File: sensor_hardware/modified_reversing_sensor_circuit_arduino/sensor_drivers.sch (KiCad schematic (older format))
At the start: 26 parts, among them Q1 S8050-J3Y, Q2 S8050-J3Y, Q3 S8050-J3Y, Q4 S8050-J3Y, U3 4052

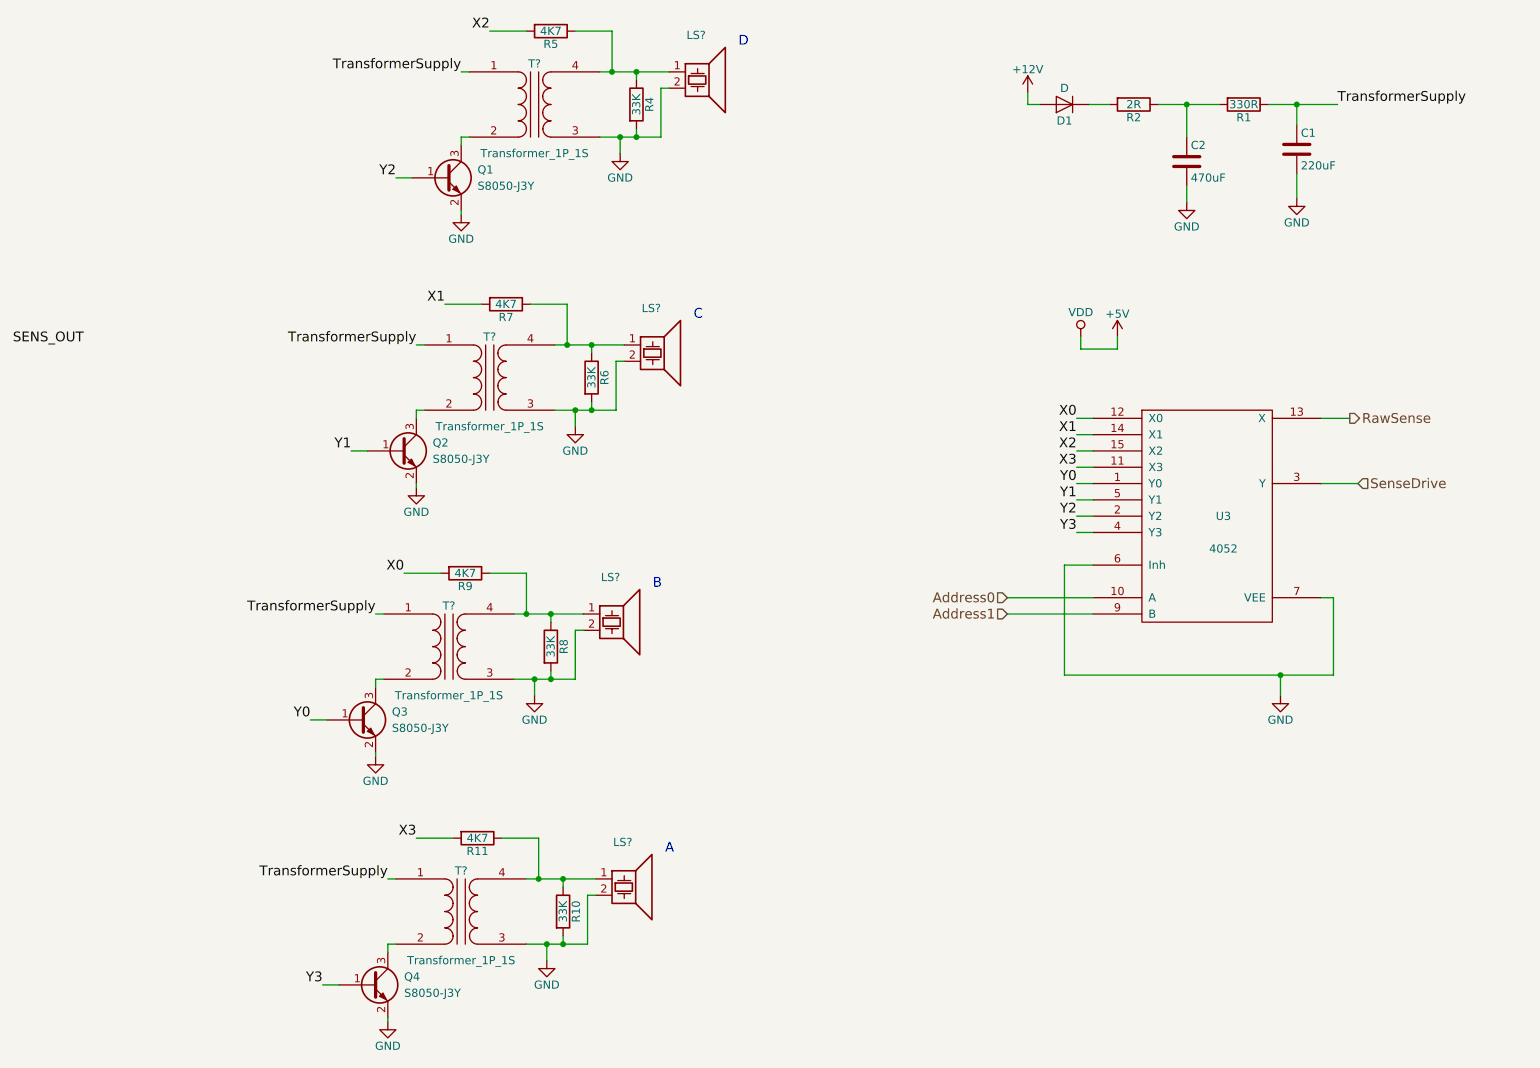
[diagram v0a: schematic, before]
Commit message: make specific atmega328 version
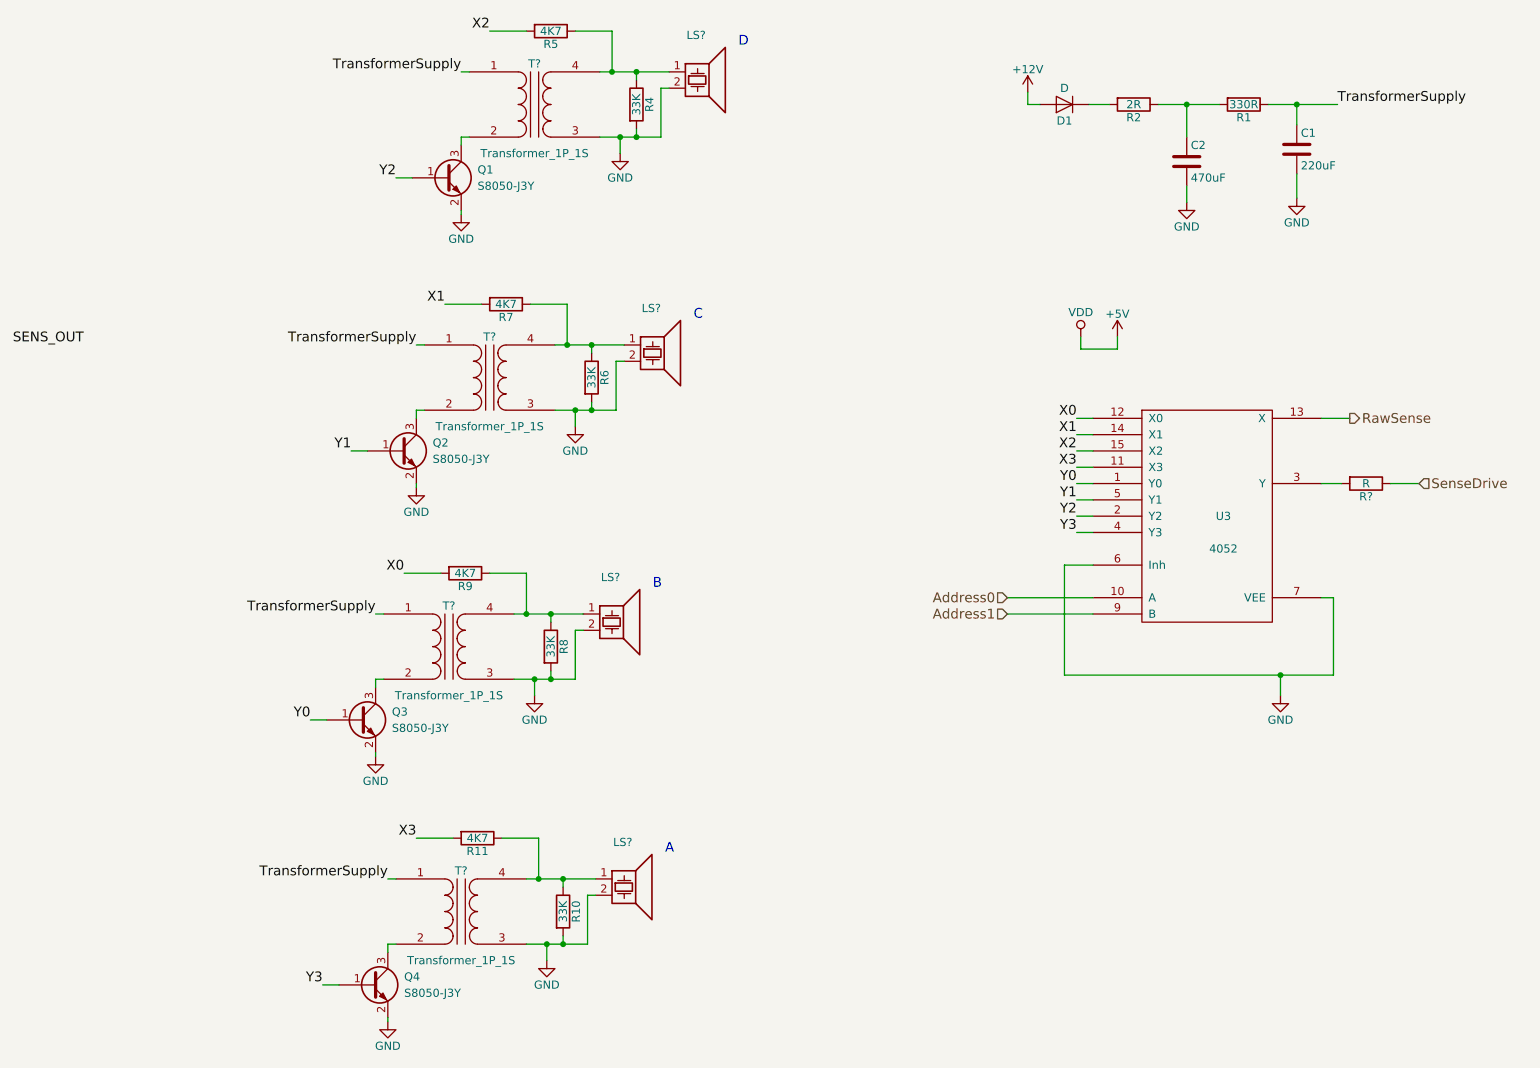
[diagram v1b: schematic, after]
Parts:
- added R?: R, symbol R
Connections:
- net SenseDrive: now also R?.1; no longer U3.3 (Y)
- new net: R?.2, U3.3 (Y)
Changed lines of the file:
@@
 LIBS:contrib
 LIBS:valves
+LIBS:atmega328p
 LIBS:reversing_sensor_circuit-cache
 EELAYER 25 0
@@
 $Descr A4 11693 8268
 encoding utf-8
-Sheet 2 3
+Sheet 2 4
 Title ""
 Date ""
@@
 $EndComp
 Wire Wire Line
-	7725 1300 8150 1300
+	7725 1300 7900 1300
+Wire Wire Line
+	7900 1300 8150 1300
 Wire Wire Line
 	7900 1300 7900 1425
 Wire Wire Line
-	7050 1300 7425 1300
+	7050 1300 7225 1300
+Wire Wire Line
+	7225 1300 7425 1300
 Wire Wire Line
 	7225 1300 7225 1500
@@
 $EndComp
 Wire Wire Line
-	3625 1500 4000 1500
+	3625 1500 3750 1500
+Wire Wire Line
+	3750 1500 3850 1500
+Wire Wire Line
+	3850 1500 4000 1500
 Wire Wire Line
 	3750 1500 3750 1600
 Wire Wire Line
-	3625 1100 4050 1100
+	3625 1100 3700 1100
+Wire Wire Line
+	3700 1100 3850 1100
+Wire Wire Line
+	3850 1100 4050 1100
 Wire Wire Line
 	4000 1500 4000 1200
@@
 $EndComp
 Wire Wire Line
-	3350 3175 3725 3175
+	3350 3175 3475 3175
+Wire Wire Line
+	3475 3175 3575 3175
+Wire Wire Line
+	3575 3175 3725 3175
 Wire Wire Line
 	3475 3175 3475 3275
 Wire Wire Line
-	3350 2775 3775 2775
+	3350 2775 3425 2775
+Wire Wire Line
+	3425 2775 3575 2775
+Wire Wire Line
+	3575 2775 3775 2775
 Wire Wire Line
 	3725 3175 3725 2875
@@
 $EndComp
 Wire Wire Line
-	3100 4825 3475 4825
+	3100 4825 3225 4825
+Wire Wire Line
+	3225 4825 3325 4825
+Wire Wire Line
+	3325 4825 3475 4825
 Wire Wire Line
 	3225 4825 3225 4925
 Wire Wire Line
-	3100 4425 3525 4425
+	3100 4425 3175 4425
+Wire Wire Line
+	3175 4425 3325 4425
+Wire Wire Line
+	3325 4425 3525 4425
 Wire Wire Line
 	3475 4825 3475 4525
@@
 $EndComp
 Wire Wire Line
-	3175 6450 3550 6450
+	3175 6450 3300 6450
+Wire Wire Line
+	3300 6450 3400 6450
+Wire Wire Line
+	3400 6450 3550 6450
 Wire Wire Line
 	3300 6450 3300 6550
 Wire Wire Line
-	3175 6050 3600 6050
+	3175 6050 3250 6050
+Wire Wire Line
+	3250 6050 3400 6050
+Wire Wire Line
+	3400 6050 3600 6050
 Wire Wire Line
 	3550 6450 3550 6150
@@
 Wire Wire Line
 	6650 3925 6550 3925
-Text HLabel 8275 3625 2    60   Input ~ 0
+Text HLabel 8650 3625 2    60   Input ~ 0
 SenseDrive
 Text HLabel 8225 3225 2    60   Output ~ 0
@@
 Wire Wire Line
 	8225 3225 8050 3225
-Wire Wire Line
-	8275 3625 8050 3625
 $Comp
 L GND #PWR?
@@
 	8050 4325 8125 4325
 Wire Wire Line
-	8125 4800 8125 4325
-Wire Wire Line
-	6475 4800 8125 4800
+	8125 4325 8125 4800
+Wire Wire Line
+	8125 4800 7800 4800
+Wire Wire Line
+	7800 4800 6475 4800
 Wire Wire Line
 	7800 4800 7800 4925
@@
 	1    0    0    -1
 $EndComp
+$Comp
+L R R?
+U 1 1 61413331
+P 8325 3625
+F 0 "R?" V 8405 3625 50  0000 C CNN
+F 1 "R" V 8325 3625 50  0000 C CNN
+F 2 "" V 8255 3625 50  0001 C CNN
+F 3 "" H 8325 3625 50  0001 C CNN
+	1    8325 3625
+	0    1    1    0
+$EndComp
+Wire Wire Line
+	8650 3625 8475 3625
+Wire Wire Line
+	8175 3625 8050 3625
 $EndSCHEMATC

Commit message: mods to schematic
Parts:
- gave numbers to parts that had none: 9
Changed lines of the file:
@@
 $EndComp
 $Comp
-L GND #PWR?
+L GND #PWR12
 U 1 1 60724902
 P 7225 1900
-F 0 "#PWR?" H 7225 1650 50  0001 C CNN
+F 0 "#PWR12" H 7225 1650 50  0001 C CNN
 F 1 "GND" H 7225 1750 50  0000 C CNN
 F 2 "" H 7225 1900 50  0001 C CNN
@@
 $EndComp
 $Comp
-L GND #PWR?
+L GND #PWR14
 U 1 1 60724908
 P 7900 1875
-F 0 "#PWR?" H 7900 1625 50  0001 C CNN
+F 0 "#PWR14" H 7900 1625 50  0001 C CNN
 F 1 "GND" H 7900 1725 50  0000 C CNN
 F 2 "" H 7900 1875 50  0001 C CNN
@@
 $EndComp
 Wire Wire Line
-	7725 1300 7900 1300
-Wire Wire Line
-	7900 1300 8150 1300
+	7725 1300 8150 1300
 Wire Wire Line
 	7900 1300 7900 1425
 Wire Wire Line
-	7050 1300 7225 1300
-Wire Wire Line
-	7225 1300 7425 1300
+	7050 1300 7425 1300
 Wire Wire Line
 	7225 1300 7225 1500
@@
 	7900 1875 7900 1725
 $Comp
-L +12V #PWR?
+L +12V #PWR9
 U 1 1 60724956
 P 6250 1225
-F 0 "#PWR?" H 6250 1075 50  0001 C CNN
+F 0 "#PWR9" H 6250 1075 50  0001 C CNN
 F 1 "+12V" H 6250 1365 50  0000 C CNN
 F 2 "" H 6250 1225 50  0001 C CNN
@@
 $EndComp
 $Comp
-L GND #PWR?
+L GND #PWR8
 U 1 1 607251DC
 P 3750 1600
-F 0 "#PWR?" H 3750 1350 50  0001 C CNN
+F 0 "#PWR8" H 3750 1350 50  0001 C CNN
 F 1 "GND" H 3750 1450 50  0000 C CNN
 F 2 "" H 3750 1600 50  0001 C CNN
@@
 $EndComp
 $Comp
-L Speaker_Ultrasound LS?
+L Speaker_Ultrasound LS4
 U 1 1 607251E2
 P 4250 1100
-F 0 "LS?" H 4275 1325 50  0000 R CNN
+F 0 "LS4" H 4275 1325 50  0000 R CNN
 F 1 "Speaker_Ultrasound" H 4275 1250 50  0001 R CNN
 F 2 "" H 4215 1050 50  0001 C CNN
@@
 $EndComp
 Wire Wire Line
-	3625 1500 3750 1500
-Wire Wire Line
-	3750 1500 3850 1500
-Wire Wire Line
-	3850 1500 4000 1500
+	3625 1500 4000 1500
 Wire Wire Line
 	3750 1500 3750 1600
 Wire Wire Line
-	3625 1100 3700 1100
-Wire Wire Line
-	3700 1100 3850 1100
-Wire Wire Line
-	3850 1100 4050 1100
+	3625 1100 4050 1100
 Wire Wire Line
 	4000 1500 4000 1200
@@
 	2775 1500 2775 1550
 $Comp
-L GND #PWR?
+L GND #PWR4
 U 1 1 60725207
 P 2775 1975
-F 0 "#PWR?" H 2775 1725 50  0001 C CNN
+F 0 "#PWR4" H 2775 1725 50  0001 C CNN
 F 1 "GND" H 2775 1825 50  0000 C CNN
 F 2 "" H 2775 1975 50  0001 C CNN
@@
 	2775 1975 2775 1950
 $Comp
-L GND #PWR?
+L GND #PWR7
 U 1 1 6073CE71
 P 3475 3275
-F 0 "#PWR?" H 3475 3025 50  0001 C CNN
+F 0 "#PWR7" H 3475 3025 50  0001 C CNN
 F 1 "GND" H 3475 3125 50  0000 C CNN
 F 2 "" H 3475 3275 50  0001 C CNN
@@
 $EndComp
 $Comp
-L Speaker_Ultrasound LS?
+L Speaker_Ultrasound LS3
 U 1 1 6073CE77
 P 3975 2775
-F 0 "LS?" H 4000 3000 50  0000 R CNN
+F 0 "LS3" H 4000 3000 50  0000 R CNN
 F 1 "Speaker_Ultrasound" H 4000 2925 50  0001 R CNN
 F 2 "" H 3940 2725 50  0001 C CNN
@@
 $EndComp
 Wire Wire Line
-	3350 3175 3475 3175
-Wire Wire Line
-	3475 3175 3575 3175
-Wire Wire Line
-	3575 3175 3725 3175
+	3350 3175 3725 3175
 Wire Wire Line
 	3475 3175 3475 3275
 Wire Wire Line
-	3350 2775 3425 2775
-Wire Wire Line
-	3425 2775 3575 2775
-Wire Wire Line
-	3575 2775 3775 2775
+	3350 2775 3775 2775
 Wire Wire Line
 	3725 3175 3725 2875
@@
 	2500 3175 2500 3225
 $Comp
-L GND #PWR?
+L GND #PWR3
 U 1 1 6073CE97
 P 2500 3650
-F 0 "#PWR?" H 2500 3400 50  0001 C CNN
+F 0 "#PWR3" H 2500 3400 50  0001 C CNN
 F 1 "GND" H 2500 3500 50  0000 C CNN
 F 2 "" H 2500 3650 50  0001 C CNN
@@
 	2500 3650 2500 3625
 $Comp
-L GND #PWR?
+L GND #PWR5
 U 1 1 6073CFB9
 P 3225 4925
-F 0 "#PWR?" H 3225 4675 50  0001 C CNN
+F 0 "#PWR5" H 3225 4675 50  0001 C CNN
 F 1 "GND" H 3225 4775 50  0000 C CNN
 F 2 "" H 3225 4925 50  0001 C CNN
@@
 $EndComp
 $Comp
-L Speaker_Ultrasound LS?
+L Speaker_Ultrasound LS1
 U 1 1 6073CFBF
 P 3725 4425
-F 0 "LS?" H 3750 4650 50  0000 R CNN
+F 0 "LS1" H 3750 4650 50  0000 R CNN
 F 1 "Speaker_Ultrasound" H 3750 4575 50  0001 R CNN
 F 2 "" H 3690 4375 50  0001 C CNN
@@
 $EndComp
 Wire Wire Line
-	3100 4825 3225 4825
-Wire Wire Line
-	3225 4825 3325 4825
-Wire Wire Line
-	3325 4825 3475 4825
+	3100 4825 3475 4825
 Wire Wire Line
 	3225 4825 3225 4925
 Wire Wire Line
-	3100 4425 3175 4425
-Wire Wire Line
-	3175 4425 3325 4425
-Wire Wire Line
-	3325 4425 3525 4425
+	3100 4425 3525 4425
 Wire Wire Line
 	3475 4825 3475 4525
@@
 	2250 4825 2250 4875
 $Comp
-L GND #PWR?
+L GND #PWR1
 U 1 1 6073CFDF
 P 2250 5300
-F 0 "#PWR?" H 2250 5050 50  0001 C CNN
+F 0 "#PWR1" H 2250 5050 50  0001 C CNN
 F 1 "GND" H 2250 5150 50  0000 C CNN
 F 2 "" H 2250 5300 50  0001 C CNN
@@
 	2250 5300 2250 5275
 $Comp
-L GND #PWR?
+L GND #PWR6
 U 1 1 6073D11B
 P 3300 6550
-F 0 "#PWR?" H 3300 6300 50  0001 C CNN
+F 0 "#PWR6" H 3300 6300 50  0001 C CNN
 F 1 "GND" H 3300 6400 50  0000 C CNN
 F 2 "" H 3300 6550 50  0001 C CNN
@@
 $EndComp
 $Comp
-L Speaker_Ultrasound LS?
+L Speaker_Ultrasound LS2
 U 1 1 6073D121
 P 3800 6050
-F 0 "LS?" H 3825 6275 50  0000 R CNN
+F 0 "LS2" H 3825 6275 50  0000 R CNN
 F 1 "Speaker_Ultrasound" H 3825 6200 50  0001 R CNN
 F 2 "" H 3765 6000 50  0001 C CNN
@@
 $EndComp
 Wire Wire Line
-	3175 6450 3300 6450
-Wire Wire Line
-	3300 6450 3400 6450
-Wire Wire Line
-	3400 6450 3550 6450
+	3175 6450 3550 6450
 Wire Wire Line
 	3300 6450 3300 6550
 Wire Wire Line
-	3175 6050 3250 6050
-Wire Wire Line
-	3250 6050 3400 6050
-Wire Wire Line
-	3400 6050 3600 6050
+	3175 6050 3600 6050
 Wire Wire Line
 	3550 6450 3550 6150
@@
 	2325 6450 2325 6500
 $Comp
-L GND #PWR?
+L GND #PWR2
 U 1 1 6073D141
 P 2325 6925
-F 0 "#PWR?" H 2325 6675 50  0001 C CNN
+F 0 "#PWR2" H 2325 6675 50  0001 C CNN
 F 1 "GND" H 2325 6775 50  0000 C CNN
 F 2 "" H 2325 6925 50  0001 C CNN
@@
 	8225 3225 8050 3225
 $Comp
-L GND #PWR?
+L GND #PWR13
 U 1 1 6074215A
 P 7800 4925
-F 0 "#PWR?" H 7800 4675 50  0001 C CNN
+F 0 "#PWR13" H 7800 4675 50  0001 C CNN
 F 1 "GND" H 7800 4775 50  0000 C CNN
 F 2 "" H 7800 4925 50  0001 C CNN
@@
 	8050 4325 8125 4325
 Wire Wire Line
-	8125 4325 8125 4800
-Wire Wire Line
-	8125 4800 7800 4800
-Wire Wire Line
-	7800 4800 6475 4800
+	8125 4800 8125 4325
+Wire Wire Line
+	6475 4800 8125 4800
 Wire Wire Line
 	7800 4800 7800 4925
@@
 	6650 4425 6125 4425
 $Comp
-L VDD #PWR?
+L VDD #PWR10
 U 1 1 6073B906
 P 6575 2725
-F 0 "#PWR?" H 6575 2575 50  0001 C CNN
+F 0 "#PWR10" H 6575 2575 50  0001 C CNN
 F 1 "VDD" H 6575 2875 50  0000 C CNN
 F 2 "" H 6575 2725 50  0001 C CNN
@@
 $EndComp
 $Comp
-L +5V #PWR?
+L +5V #PWR11
 U 1 1 6073B9B6
 P 6800 2725
-F 0 "#PWR?" H 6800 2575 50  0001 C CNN
+F 0 "#PWR11" H 6800 2575 50  0001 C CNN
 F 1 "+5V" H 6800 2865 50  0000 C CNN
 F 2 "" H 6800 2725 50  0001 C CNN
@@
 	6800 2800 6800 2725
 $Comp
-L Transformer_1P_1S T?
+L Transformer_1P_1S T4
 U 1 1 61362743
 P 3225 1300
-F 0 "T?" H 3225 1550 50  0000 C CNN
+F 0 "T4" H 3225 1550 50  0000 C CNN
 F 1 "Transformer_1P_1S" H 3225 1000 50  0000 C CNN
 F 2 "" H 3225 1300 50  0001 C CNN
@@
 $EndComp
 $Comp
-L Transformer_1P_1S T?
+L Transformer_1P_1S T3
 U 1 1 61362A06
 P 2950 2975
-F 0 "T?" H 2950 3225 50  0000 C CNN
+F 0 "T3" H 2950 3225 50  0000 C CNN
 F 1 "Transformer_1P_1S" H 2950 2675 50  0000 C CNN
 F 2 "" H 2950 2975 50  0001 C CNN
@@
 $EndComp
 $Comp
-L Transformer_1P_1S T?
+L Transformer_1P_1S T1
 U 1 1 61362D1D
 P 2700 4625
-F 0 "T?" H 2700 4875 50  0000 C CNN
+F 0 "T1" H 2700 4875 50  0000 C CNN
 F 1 "Transformer_1P_1S" H 2700 4325 50  0000 C CNN
 F 2 "" H 2700 4625 50  0001 C CNN
@@
 $EndComp
 $Comp
-L Transformer_1P_1S T?
+L Transformer_1P_1S T2
 U 1 1 61362EAF
 P 2775 6250
-F 0 "T?" H 2775 6500 50  0000 C CNN
+F 0 "T2" H 2775 6500 50  0000 C CNN
 F 1 "Transformer_1P_1S" H 2775 5950 50  0000 C CNN
 F 2 "" H 2775 6250 50  0001 C CNN
@@
 $EndComp
 $Comp
-L R R?
+L R R3
 U 1 1 61413331
 P 8325 3625
-F 0 "R?" V 8405 3625 50  0000 C CNN
+F 0 "R3" V 8405 3625 50  0000 C CNN
 F 1 "R" V 8325 3625 50  0000 C CNN
 F 2 "" V 8255 3625 50  0001 C CNN
